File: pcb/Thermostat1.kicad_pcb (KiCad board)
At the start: 2 copper layers, 100 x 100 mm, 28 parts, among them J1 Barrel_Jack, J2 Conn_01x04_Female, J3 Screw_Terminal_01x02, K1 HK19F-DC_12-SHG, Q1 2N3904, SW1 SW_Push, SW2 SW_Push, SW3 SW_Push, SW4 SW_Push, SW5 SW_Push, U1 DS18B20

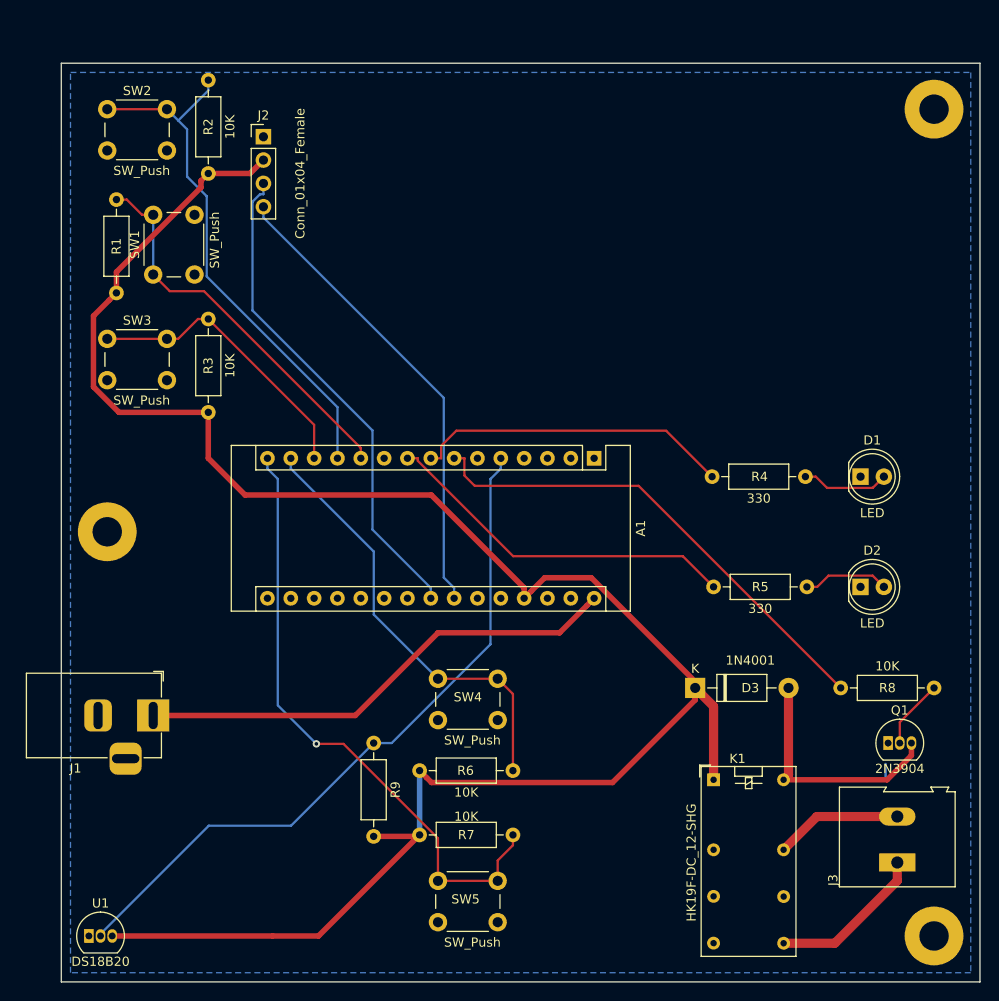
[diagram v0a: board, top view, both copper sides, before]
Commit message: New revision of pcb with updates suggested by Steve P.
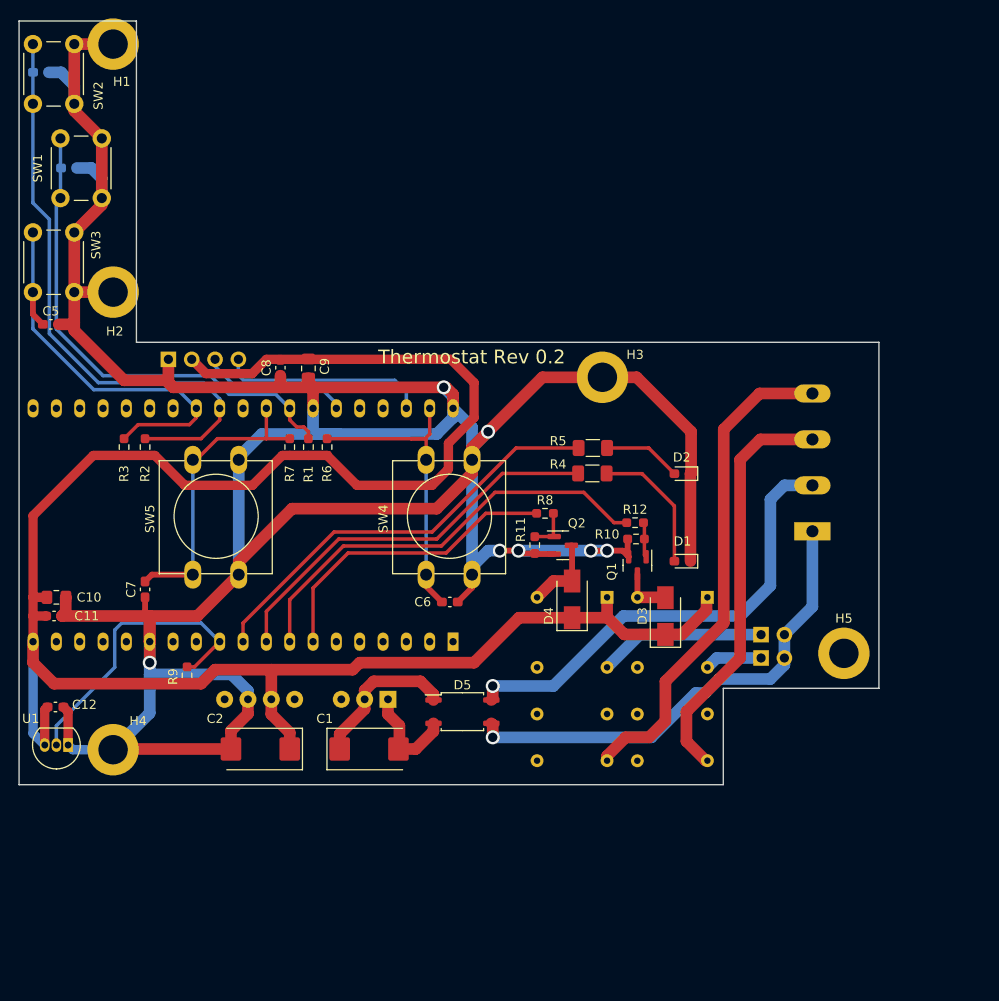
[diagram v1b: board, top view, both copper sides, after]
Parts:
- removed A1: Arduino_Nano_v3.x, Module:Arduino_Nano
- removed G***: LOGO, logos:LOGO
- removed J3: Screw_Terminal_01x02, TerminalBlock:TerminalBlock_Altech_AK300-2_P5.00mm
- removed REF** (x3): MountingHole_3.2mm_M3_Pad, MountingHole:MountingHole_3.2mm_M3_Pad
- added C1: 100uF?, Capacitor_Tantalum_SMD:CP_EIA-7343-43_Kemet-X_Pad2.25x2.55mm_HandSolder, F.Cu at (63.5, 104.6)
- added C10: 0.1u, Capacitor_SMD:C_0805_2012Metric_Pad1.18x1.45mm_HandSolder, F.Cu at (29.5, 88.1)
- added C11: 10000p, Capacitor_SMD:C_0603_1608Metric_Pad1.08x0.95mm_HandSolder, F.Cu at (29.2, 90.2)
- added C12: 10000p, Capacitor_SMD:C_0603_1608Metric_Pad1.08x0.95mm_HandSolder, F.Cu at (29.4, 100.1)
- added C2: 10uF?, Capacitor_Tantalum_SMD:CP_EIA-7343-43_Kemet-X_Pad2.25x2.55mm_HandSolder, F.Cu at (51.7, 104.6)
- added C3: 10000p, Capacitor_SMD:C_0603_1608Metric_Pad1.08x0.95mm_HandSolder, B.Cu at (30.8, 41.4)
- added C4: 10000p, Capacitor_SMD:C_0603_1608Metric_Pad1.08x0.95mm_HandSolder, B.Cu at (27.8, 31.0)
- added C5: 10000p, Capacitor_SMD:C_0603_1608Metric_Pad1.08x0.95mm_HandSolder, F.Cu at (28.9, 58.4)
- added C6: 10000p, Capacitor_SMD:C_0603_1608Metric_Pad1.08x0.95mm_HandSolder, F.Cu at (72.3, 88.6)
- added C7: 10000p, Capacitor_SMD:C_0603_1608Metric_Pad1.08x0.95mm_HandSolder, F.Cu at (39.1, 87.3)
- added C8: 10000p, Capacitor_SMD:C_0603_1608Metric_Pad1.08x0.95mm_HandSolder, F.Cu at (53.8, 63.1)
- added C9: 0.1u, Capacitor_SMD:C_0805_2012Metric_Pad1.18x1.45mm_HandSolder, F.Cu at (56.9, 63.2)
- added D4: S1A, Diode_SMD:D_SMA, F.Cu at (85.6, 88.4)
- added D5: HD02-T, Package_SO:SO-4_4.4x3.9mm_P2.54mm, F.Cu at (73.7, 100.6)
- added H1: MountingHole_Pad, MountingHole:MountingHole_3.2mm_M3_DIN965_Pad, F.Cu at (35.6, 27.9)
- added H2: MountingHole_Pad, MountingHole:MountingHole_3.2mm_M3_DIN965_Pad, F.Cu at (35.6, 54.9)
- added H3: MountingHole_Pad, MountingHole:MountingHole_3.2mm_M3_DIN965_Pad, F.Cu at (88.9, 64.2)
- added H4: MountingHole_Pad, MountingHole:MountingHole_3.2mm_M3_DIN965_Pad, F.Cu at (35.6, 104.7)
- added H5: MountingHole_Pad, MountingHole:MountingHole_3.2mm_M3_DIN965_Pad, F.Cu at (115.2, 94.2)
- added JP1: Jumper_2_Bridged, Connector_PinHeader_2.54mm:PinHeader_1x02_P2.54mm_Vertical, B.Cu at (106.2, 94.7)
- added JP2: Jumper_2_Bridged, Connector_PinHeader_2.54mm:PinHeader_1x02_P2.54mm_Vertical, B.Cu at (106.2, 92.2)
- added K2: HK19F-DC_12-SHG, Relay_THT:Relay_DPDT_Omron_G5V-2, B.Cu at (89.4, 88.1)
- added PS1: URB4805S-3WR3, Converter_DCDC:Converter_DCDC_XP_POWER-ITxxxxxS_THT, B.Cu at (65.6, 99.2)
- added Q2: SI2310B, Package_TO_SOT_SMD:SOT-23, F.Cu at (84.6, 82.5)
- added R10: 10K, Resistor_SMD:R_0603_1608Metric_Pad0.98x0.95mm_HandSolder, F.Cu at (92.6, 81.8)
- added R11: 10K, Resistor_SMD:R_0603_1608Metric_Pad0.98x0.95mm_HandSolder, F.Cu at (81.5, 82.4)
- added R12: 100, Resistor_SMD:R_0603_1608Metric_Pad0.98x0.95mm_HandSolder, F.Cu at (92.5, 80.0)
- added U2: ESP32-DevKitC, Espressif:ESP32-DevKitC, B.Cu at (72.6, 93.0)
- D1, D2: footprint LED_THT:LED_D5.0mm -> LED_SMD:LED_0603_1608Metric_Pad1.05x0.95mm_HandSolder
- D3: value 1N4001 -> S1A; footprint Diode_THT:D_DO-41_SOD81_P10.16mm_Horizontal -> Diode_SMD:D_SMA
- J1: value Barrel_Jack -> Screw_Terminal_01x04; footprint Connector_BarrelJack:BarrelJack_Horizontal -> TerminalBlock:TerminalBlock_Altech_AK300-4_P5.00mm; moved to B.Cu
- J2, K1: moved to B.Cu
- Q1: value 2N3904 -> SI2310B; footprint Package_TO_SOT_THT:TO-92_Inline -> Package_TO_SOT_SMD:SOT-23
- R1, R2, R3, R6, R7, R9: footprint Resistor_THT:R_Axial_DIN0207_L6.3mm_D2.5mm_P10.16mm_Horizontal -> Resistor_SMD:R_0603_1608Metric_Pad0.98x0.95mm_HandSolder
- R4, R5: footprint Resistor_THT:R_Axial_DIN0207_L6.3mm_D2.5mm_P10.16mm_Horizontal -> Resistor_SMD:R_1206_3216Metric_Pad1.30x1.75mm_HandSolder
- R8: value 10K -> 100; footprint Resistor_THT:R_Axial_DIN0207_L6.3mm_D2.5mm_P10.16mm_Horizontal -> Resistor_SMD:R_0603_1608Metric_Pad0.98x0.95mm_HandSolder
- SW4, SW5: footprint Button_Switch_THT:SW_PUSH_6mm -> Button_Switch_THT:SW_PUSH-12mm
- moved J1 74.5 mm to (111.8, 80.9), turned to 90 degrees
- moved R8 46.4 mm to (82.7, 79.0), turned to 0 degrees
- moved R7 44.5 mm to (54.9, 71.8), turned to 90 degrees
- moved SW5 42.7 mm to (44.3, 85.7), turned to 90 degrees
- moved R6 36.6 mm to (58.9, 71.8), turned to 90 degrees
- moved Q1 33.4 mm to (92.7, 84.7), turned to -90 degrees
- moved R2 30.6 mm to (39.1, 71.8)
- moved R1 26.8 mm to (56.9, 71.8)
- moved J2 26.3 mm to (41.7, 62.2), turned to -90 degrees
- moved D2 23.0 mm to (97.6, 74.7), turned to 180 degrees
- moved R9 21.6 mm to (43.7, 96.6)
- moved D1 21.5 mm to (97.6, 84.2), turned to 180 degrees
- moved U1 20.9 mm to (30.7, 104.2), turned to 180 degrees
- moved R5 20.0 mm to (87.9, 71.9)
- moved K1 19.9 mm to (100.3, 88.1), turned to 180 degrees
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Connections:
- net /CANCEL_SWITCH renamed /SWITCH1
- net /RELAY_PULLDOWN renamed Net-(D3-Pad2)
- net /START_SWITCH renamed /SWITCH0
- J1 pad 1: /VIN -> /VACHOT
- J1 pad 2: GND -> /VACCOM
- J1 pad 3: (no net) -> /RELAY_OUTA0
- K1 pad 11: Net-(K1-Pad11) -> unconnected-(K1-Pad11)
- K1 pad 13: /RELAY_OUTB -> unconnected-(K1-Pad13)
- K1 pad 4: Net-(K1-Pad4) -> /RELAY_OUTB0
- K1 pad 6: Net-(K1-Pad6) -> unconnected-(K1-Pad6)
- K1 pad 8: Net-(K1-Pad8) -> /RELAY_OUTA0
- K1 pad 9: /RELAY_OUTA -> unconnected-(K1-Pad9)
- Q1 pad 1: GND -> Net-(Q1-Pad1)
- Q1 pad 2: Net-(Q1-Pad2) -> GND
- R4 pad 1: /HEATING_LED -> /LED0
- R5 pad 1: /OVERRIDE_LED -> /LED1
- R8 pad 1: Net-(Q1-Pad2) -> /RELAY_DRIVE1
- R8 pad 2: /RELAY_DRIVE -> Net-(Q2-Pad1)
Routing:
- net GND: track 1.73 -> 374.6 mm, vias 0 -> 7
- net /RELAY_OUTA1: track 0.00 -> 54.1 mm
- net /RELAY_DRIVE: track 53.5 -> 0.00 mm
- net /VIN: track 53.3 -> 0.00 mm
- net /VACHOT: track 0.00 -> 52.4 mm, vias 0 -> 1
- net /VACCOM: track 0.00 -> 50.9 mm, vias 0 -> 1
- net /RELAY_DRIVE0: track 0.00 -> 47.6 mm
- net /LED1: track 0.00 -> 46.4 mm
- net /RELAY_OUTA0: track 0.00 -> 44.9 mm
- net /TEMP_DATA: track 76.7 -> 32.4 mm
- net /LED0: track 0.00 -> 43.5 mm
- net /OVERRIDE_LED: track 39.3 -> 0.00 mm
- net /SDA: track 53.9 -> 15.4 mm
- net /SWITCH1: track 67.6 -> 32.8 mm, vias 1 -> 0
- net /HEATING_LED: track 34.7 -> 0.00 mm
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- removed copper zone on B.Cu, net GND
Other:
- board size 100 x 100 mm -> 93.6 x 83.1 mm
- net class Default removed
- board text added: "Thermostat Rev 0.2"
- board text removed: "Thermostat Rev 0.1"

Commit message: Fixed a couple issues on schematic and layout - swapped power supplies on external components and pullups from 5V to 3.3V, moved input connector so it's further from the edge of the box, increased spacing on thermometer leads to accomodate available parts and added an FCCH logo.
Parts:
- added C13: 1.0u, Capacitor_SMD:C_0805_2012Metric_Pad1.18x1.45mm_HandSolder, B.Cu at (52.6, 77.2)
- added C14: 22000p, Capacitor_SMD:C_0603_1608Metric_Pad1.08x0.95mm_HandSolder, B.Cu at (52.7, 80.5)
- added R13: DNP, Resistor_SMD:R_0603_1608Metric_Pad0.98x0.95mm_HandSolder, F.Cu at (62.0, 71.7)
- added R14: DNP, Resistor_SMD:R_0603_1608Metric_Pad0.98x0.95mm_HandSolder, F.Cu at (59.9, 71.7)
- added REF**: fcch-logo, projectlib:fcch-logo, F.Cu at (33.0, 86.6)
- C1: value 100uF? -> 10uF, 50V
- C10, C9: value 0.1u -> 1.0u
- C11, C12, C3, C4, C5, C6, C7, C8: value 10000p -> 22000p
- C2: value 10uF? -> 150uF, 16V
- D1: value LED -> 150080VS75000
- D2: value LED -> 150080SS75000
- R4: value 330 -> 63.4
- R5: value 330 -> 118
- R9: value 4.7K -> 4.87K; moved to B.Cu
- U1: footprint Package_TO_SOT_THT:TO-92_Inline -> Package_TO_SOT_THT:TO-92_Inline_Wide
- moved R9 14.0 mm to (29.7, 96.8), turned to 180 degrees
- moved J1 5.08 mm to (106.7, 80.9)
- moved R6 5.08 mm to (64.0, 71.8)
- moved C12 3.41 mm to (32.8, 100.3), turned to -90 degrees
- moved U1 1.28 mm to (29.5, 104.4), turned to 90 degrees
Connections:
- C12 pad 1: +5V -> +3.3V
- R1 pad 1: +5V -> +3.3V
- R2 pad 1: +5V -> +3.3V
- R3 pad 1: +5V -> +3.3V
- R6 pad 1: +5V -> +3.3V
- R7 pad 1: +5V -> +3.3V
- R9 pad 2: +5V -> +3.3V
- U1 pad 3: +5V -> +3.3V
- U2 pad 1: unconnected-(U2-Pad1) -> +3.3V
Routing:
- net +3.3V: track 0.00 -> 115.4 mm, vias 0 -> 2
- net +5V: track 223.5 -> 198.2 mm
- net /SCL: track 21.8 -> 29.9 mm
- net /SWITCH0: track 34.3 -> 29.2 mm
- net GND: track 374.6 -> 379.4 mm
- net /VACCOM: track 50.9 -> 46.6 mm
- net /TEMP_DATA: track 32.4 -> 28.1 mm
- net /RELAY_OUTA0: track 44.9 -> 41.2 mm
- net /SDA: track 15.4 -> 18.7 mm
- net /RELAY_OUTA1: track 54.1 -> 51.0 mm
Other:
- board text added: "Creator Hub"
- board text added: "Fort Collins"
- board text added: "OUT0"
- board text added: "OUT1"
- board text added: "Thermostat Rev 0.3"
- board text added: "VACCOM"
- board text added: "VACHOT"
- board text removed: "Thermostat Rev 0.2"

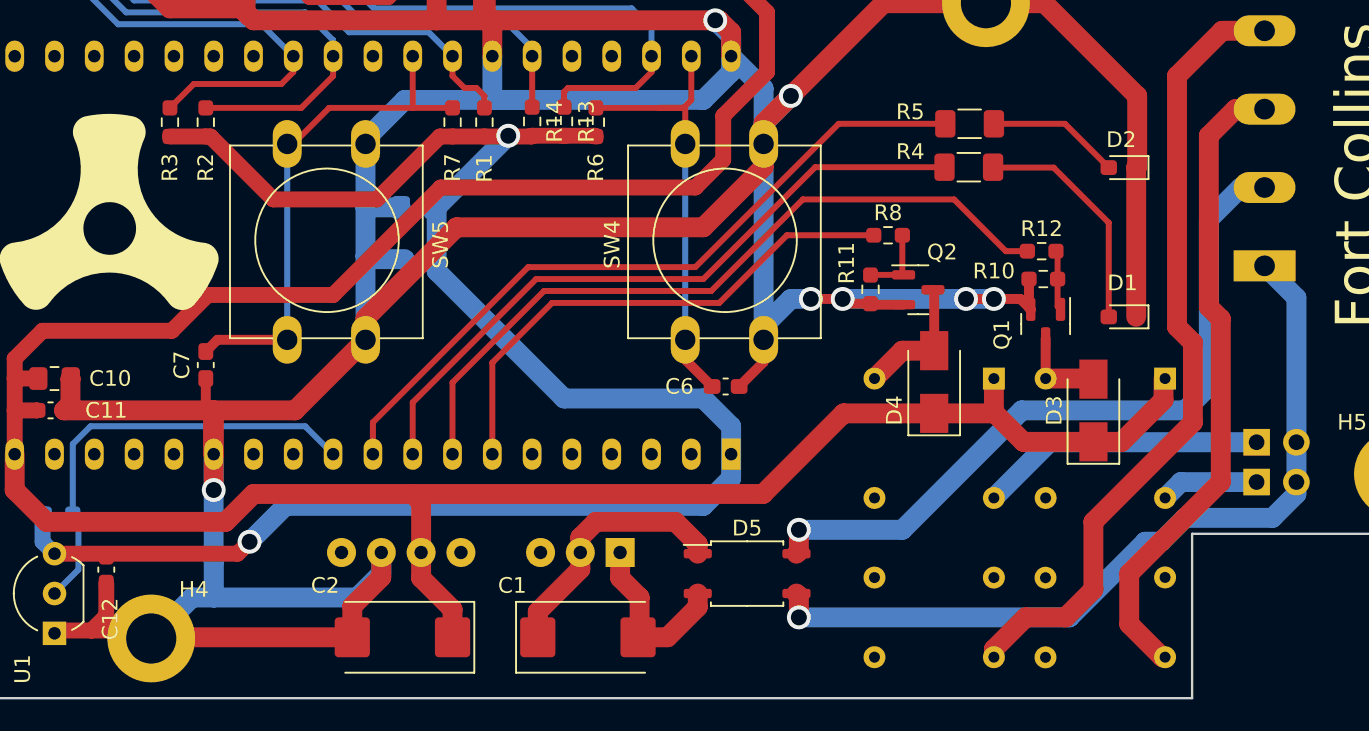
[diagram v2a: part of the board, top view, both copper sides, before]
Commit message: A few more fixes for Rev 0.3 - more options for power input caps as well as some sense resistors, also remade gerber files.
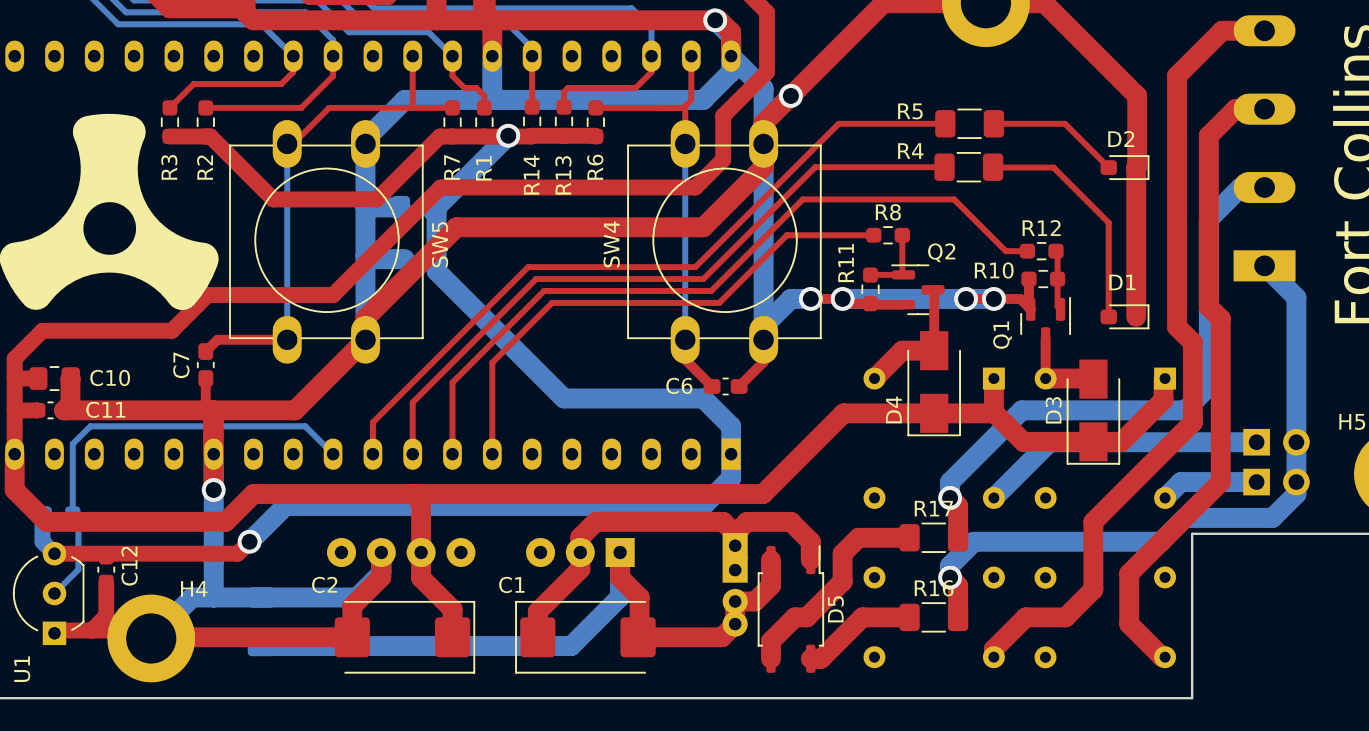
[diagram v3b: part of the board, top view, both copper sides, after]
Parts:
- added C15: 10uF, 50V, Capacitor_THT:CP_Radial_D5.0mm_P2.00mm, B.Cu at (72.9, 100.4)
- added C16: 10uF, 50V, Capacitor_THT:CP_Radial_D8.0mm_P5.00mm, B.Cu at (72.9, 98.8)
- added R15: DNP, Resistor_SMD:R_1206_3216Metric_Pad1.30x1.75mm_HandSolder, B.Cu at (42.7, 103.7)
- added R16: 10, Resistor_SMD:R_1206_3216Metric_Pad1.30x1.75mm_HandSolder, F.Cu at (85.6, 103.4)
- added R17: 10, Resistor_SMD:R_1206_3216Metric_Pad1.30x1.75mm_HandSolder, F.Cu at (85.6, 98.3)
- moved D5 3.61 mm to (76.5, 102.9), turned to -90 degrees
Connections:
- D5 pad 3: /VACHOT -> Net-(D5-Pad3)
- D5 pad 4: /VACCOM -> Net-(D5-Pad4)
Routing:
- net Net-(C1-Pad2): track 11.4 -> 45.3 mm
- net Net-(D5-Pad3): track 0.00 -> 13.7 mm
- net Net-(C1-Pad1): track 16.6 -> 27.3 mm
- net /VACHOT: track 52.0 -> 42.9 mm
- net /VACCOM: track 46.6 -> 37.9 mm
- net Net-(D5-Pad4): track 0.00 -> 7.39 mm
